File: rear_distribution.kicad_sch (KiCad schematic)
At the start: 42 parts, among them J1 Conn_01x23, J10 Conn_01x02, J11 Conn_01x02, J12 Conn_01x02, J13 Conn_01x04, J14 Conn_01x02, J15 Conn_01x04, J16 Conn_01x23, J17 Conn_01x35, J2 Conn_01x02, J3 Conn_01x02, J4 Conn_01x04, J5 Conn_01x03, J6 Conn_01x08, J7 Conn_01x23, J8 Conn_01x08, J9 Conn_01x08, K1 G2RL-1A, Q1 DMN61D8LQ

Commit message: schematic: Tentatively finish major schematic parts
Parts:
- removed J1: Conn_01x23, yfs:AMPSEAL-23-776087, symbol Connector_Generic:Conn_01x23
- removed NT1: NetTie_4_Cross, symbol Device:NetTie_4_Cross
- removed NT2: NetTie_2, symbol Device:NetTie_2
- removed Q1: DMN61D8LQ, Package_TO_SOT_SMD:SOT-23, symbol Transistor_FET:DMN61D8LQ
- added J21: Conn_01x23, yfs:AMPSEAL-23-776087, symbol Connector_Generic:Conn_01x23
- added NT1: NetTie_2, symbol Device:NetTie_2
- added NT3: NetTie_3_Tee, symbol Device:NetTie_3_Tee
- added Q1, Q4: DMN6075S, Package_TO_SOT_SMD:SOT-23, symbol Transistor_FET:DMN6075S
- added R43, R46, R55, R56: 10k, symbol Device:R_Small
- added R44, R45: 100, symbol Device:R_Small
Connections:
- net +12V: now also NT1.1
- net 12V_BMS: now also J16.5 (Pin_5); no longer J16.19 (Pin_19)
- net 12V_BRAKE_LIGHT: now also F17.2
- net 12V_DTI: now also J21.1 (Pin_1), J21.5 (Pin_5), J21.9 (Pin_9)
- net 12V_FAN: now also J16.4 (Pin_4); no longer J16.20 (Pin_20)
- net 12V_HV_DET: now also J16.3 (Pin_3); no longer J16.21 (Pin_21)
- net 12V_IMD: now also J16.2 (Pin_2); no longer J16.22 (Pin_22)
- net 12V_PRCHG: now also J16.1 (Pin_1); no longer J16.23 (Pin_23)
- net 5V_TSAL: now also J16.6 (Pin_6); no longer J16.18 (Pin_18)
- net AIR+_ACT: now also J16.19 (Pin_19); no longer J16.5 (Pin_5)
- net AIR+_INT: now also J16.18 (Pin_18); no longer J16.6 (Pin_6)
- net AIR-_ACT: now also J16.17 (Pin_17); no longer J16.7 (Pin_7)
- net AIR-_INT: now also J16.16 (Pin_16); no longer J16.8 (Pin_8)
- net BMS_OK: now also J16.10 (Pin_10); no longer J16.14 (Pin_14)
- net BRAKE_SWITCH_IN: now also NT1.2; no longer F17.2
- net CANH: now also J16.7 (Pin_7), J21.12 (Pin_12); no longer J16.17 (Pin_17)
- net CANH_DTI: now also J21.11 (Pin_11)
- net CANL: now also J16.8 (Pin_8), J21.4 (Pin_4); no longer J16.16 (Pin_16)
- net CANL_DTI: now also J21.3 (Pin_3)
- net DISCHG: now also J16.13 (Pin_13); no longer J16.11 (Pin_11)
- net DTI_OK: now also J21.13 (Pin_13)
- net GND: now also J16.21 (Pin_21), J16.22 (Pin_22), J16.23 (Pin_23), J21.16 (Pin_16), J21.17 (Pin_17), NT3.3, Q1.2 (S), Q4.2 (S), R43.2, R46.2; no longer J16.1 (Pin_1), J16.2 (Pin_2), J16.3 (Pin_3)
- net GND_BRAKE_LIGHT: now also Q4.3 (D)
- net GND_COOLANT: now also NT3.1
- net GND_TSAL_LED: now also NT3.2
- net HV_DET: now also J16.20 (Pin_20); no longer J16.4 (Pin_4)
- net IMD_OK: now also J16.11 (Pin_11); no longer J16.13 (Pin_13)
- net MCU_COOLANT: now also R45.1, R46.1
- net PRCHG_ACT: now also J16.15 (Pin_15); no longer J16.9 (Pin_9)
- net PRCHG_INT: now also J16.14 (Pin_14); no longer J16.10 (Pin_10)
- net SDN_TSAC_IN: now also J16.9 (Pin_9); no longer J16.15 (Pin_15)
- net at D1.2 (A), K1.A2: now also Q1.3 (D)
- new net: Q4.1 (G), R44.2
- new net: Q1.1 (G), R45.2
- new net +3V3: R55.1, R56.1
- new net DTI_IN_1: J21.21 (Pin_21)
- new net DTI_IN_2: J21.22 (Pin_22)
- new net DTI_OUT_1: J21.19 (Pin_19), R55.2
- new net DTI_OUT_2: J21.20 (Pin_20), R56.2
- new net MCU_BRAKE: R43.1, R44.1
- no-connect marks 23 -> 19
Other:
- removed sheet Divider10
- removed sheet Divider11
- removed sheet Divider12
- removed sheet Divider13
- removed sheet Divider14
- removed sheet Divider15
- removed sheet Divider16
- removed sheet Divider17
- removed sheet Divider18
- removed sheet Divider19
- removed sheet Divider6
- removed sheet Divider7
- removed sheet Divider8
- removed sheet Divider9
- sheet Divider ports: added IN1, IN2, IN3, IN4, OUT1, OUT2, OUT3, OUT4; removed IN, OUT
- sheet Divider1 ports: added IN1, IN2, IN3, IN4, OUT1, OUT2, OUT3, OUT4; removed IN, OUT
- sheet Divider2 ports: added IN1, IN2, IN3, IN4, OUT1, OUT2, OUT3, OUT4; removed IN, OUT
- sheet Divider3 ports: added IN1, IN2, IN3, IN4, OUT1, OUT2, OUT3, OUT4; removed IN, OUT
- sheet Divider4 ports: added IN1, IN2, IN3, IN4, OUT1, OUT2, OUT3, OUT4; removed IN, OUT
- sheet Divider5 ports: added IN1, IN2, IN3, IN4, OUT1, OUT2, OUT3, OUT4; removed IN, OUT
- sheet Microcontroller ports: added BMS_OK_SAMPLE, DISCHG_SAMPLE, DTI_OK_SAMPLE, IMD_OK_SAMPLE, SDN_FRONT_SAMPLE; removed SDN_DTI_SAMPLE
- note added: "BSPD Input"
- note added: "Brake Light Switching"
- note added: "Coolant Pump Switching"
- note removed: "BSPD"
- note removed: "Brake Light Activation"
- note removed: "Connect any spare MCU GPIO"
- note removed: "Coolant Pump"
- note removed: "Could sample BMS_OK and IMD_OK if spare GPIO"
- note removed: "Measure discharge?"
- note removed: "TODO: Switch to resistor arrays"
- company: (none) -> York Formula Student
- title: (none) -> Rear Distribution
- moved on the sheet: D1, F1, F10, F11, F12, F13, F14, F15, F16, F17, F18, F20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

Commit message: schematic: Re-annotate and add RTC battery
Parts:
- renumbered D1 to D7, F20 to F11, F17 to F12, F18 to F13, F3 to F21, F4 to F22, F5 to F23, F6 to F24, F7 to F25, F8 to F26, F9 to F27, F13 to F31, F14 to F32, F15 to F33, F16 to F34, F1 to F41, F11 to F51, F10 to F61, F12 to F81, F2 to F91, J17 to J11, J7 to J21, J16 to J31, J21 to J41, J9 to J51, J8 to J61, J10 to J71, J11 to J81, J12 to J82, J13 to J83, J15 to J84, J14 to J85, J2 to J91, J3 to J92, J4 to J93, J5 to J94, J6 to J95, JP1 to JP61, NT3 to NT1, NT1 to NT2, Q4 to Q1, Q1 to Q2, R55 to R11, R56 to R12, R43 to R13, R44 to R14, R46 to R15, R45 to R16
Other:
- note removed: "Should MCU measure UPS output directly?"
- moved on the sheet: F51, F61, J51, J61, JP61

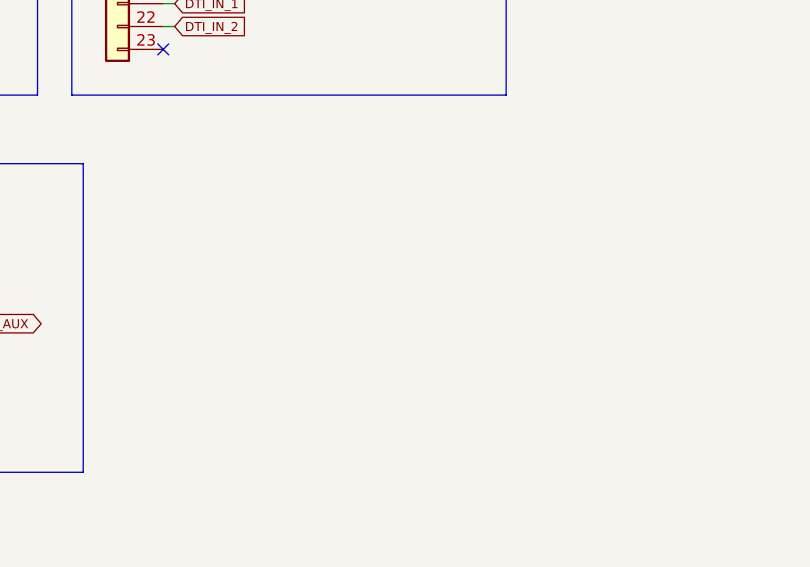
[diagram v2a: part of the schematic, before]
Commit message: schematic: Assign footprints and fill most of BOM
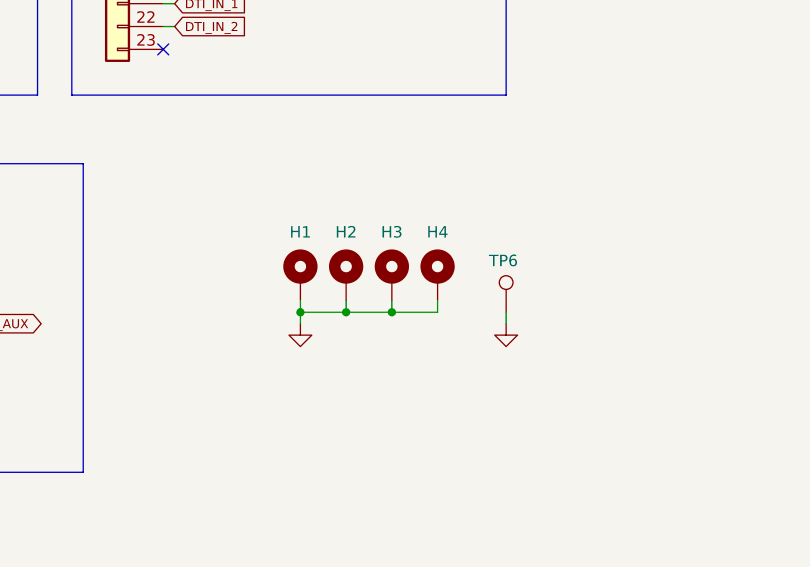
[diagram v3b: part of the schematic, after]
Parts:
- added H1, H2, H3, H4: MountingHole_Pad, MountingHole:MountingHole_3.2mm_M3_Pad_Via, symbol Mechanical:MountingHole_Pad
- added TP6: TestPoint, TestPoint:TestPoint_Keystone_5019_Miniature, symbol Connector:TestPoint
- F11, F12, F13, F21, F22, F23, F24, F25, F26, F27, F31, F32, F33, F34, F41, F51, F61, F81, F91: footprint (none) -> yfs:Keystone_3557-2; DigiKey # (none) -> 36-3557-2-ND; LCSC # (none) -> C352820; Mfr (none) -> Keystone Electronics; Mfr # (none) -> 3557-2; Mouser # (none) -> 534-3557-2
- J11: footprint (none) -> yfs:AMPSEAL-35-776163; DigiKey # (none) -> A106460-ND; Mfr (none) -> TE Connectivity; Mfr # (none) -> 776163-1; Mouser # (none) -> 571-776163-1
- J21, J31, J41: DigiKey # (none) -> A107007-ND; Mfr (none) -> TE Connectivity; Mfr # (none) -> 776087-1; Mouser # (none) -> 571-776087-1
- J51, J61: footprint (none) -> yfs:AMPSEAL-8-776280; DigiKey # (none) -> 776280-1-ND; Mfr (none) -> TE Connectivity; Mfr # (none) -> 776280-1; Mouser # (none) -> 571-776280-1
- J71, J82: footprint (none) -> yfs:MolexMicrofitPlus1x2; DigiKey # (none) -> 900-2157601032-ND; Mfr (none) -> Molex; Mfr # (none) -> 2157601032; Mouser # (none) -> 538-215760-1032
- J81, J91: footprint (none) -> yfs:MolexMicrofitPlus1x2; DigiKey # (none) -> 900-2157601022-ND; Mfr (none) -> Molex; Mfr # (none) -> 2157601022; Mouser # (none) -> 538-215760-1022
- J83, J84, J93: footprint (none) -> yfs:MolexMicrofitPlus1x4; DigiKey # (none) -> 900-2157601004-ND; Mfr (none) -> Molex; Mfr # (none) -> 2157601004; Mouser # (none) -> 538-215760-1004
- J85, J92: footprint (none) -> yfs:MolexMicrofitPlus1x2; DigiKey # (none) -> 900-2157601002-ND; Mfr (none) -> Molex; Mfr # (none) -> 2157601002; Mouser # (none) -> 538-215760-1002
- J94: footprint (none) -> yfs:MolexMicrofitPlus1x3; DigiKey # (none) -> 900-2157601003-ND; Mfr (none) -> Molex; Mfr # (none) -> 2157601003; Mouser # (none) -> 538-215760-1003
- J95: footprint (none) -> yfs:MolexMicrofitPlus1x8; DigiKey # (none) -> 900-2157601008-ND; Mfr (none) -> Molex; Mfr # (none) -> 2157601008; Mouser # (none) -> 538-215760-1008
- JP61: footprint (none) -> Jumper:SolderJumper-2_P1.3mm_Open_RoundedPad1.0x1.5mm
- K1: DigiKey # (none) -> Z140-ND; Mfr (none) -> Omron; Mfr # (none) -> G2RL-1A-DC12; Mouser # (none) -> 653-G2RL-1A-DC12
- NT1: footprint (none) -> NetTie:NetTie-3_SMD_Pad0.5mm
- NT2: footprint (none) -> NetTie:NetTie-2_SMD_Pad0.5mm
- R11, R12, R13, R15: footprint (none) -> Resistor_SMD:R_0603_1608Metric; LCSC # (none) -> C25804; Mfr (none) -> Uni-Royal; Mfr # (none) -> 0603WAF1002T5E
- R14, R16: footprint (none) -> Resistor_SMD:R_0603_1608Metric
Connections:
- net GND: now also H1.1, H2.1, H3.1, H4.1, TP6.1

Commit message: *: Setup PCB
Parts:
- added NT10, NT3, NT4, NT5, NT6, NT7, NT8, NT9: NetTie_2, NetTie:NetTie-2_SMD_Pad0.5mm, symbol Device:NetTie_2
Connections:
- net SDN_AUX_IN: now also NT8.2; no longer J51.3 (Pin_3)
- net SDN_AUX_OUT: now also NT9.1; no longer J11.31 (Pin_31)
- net SDN_BSPD_OUT: now also NT3.1; no longer J21.10 (Pin_10)
- net SDN_FRONT_OUT: now also NT4.1; no longer J82.2 (Pin_2)
- net SDN_HVD_IN: now also NT7.2; no longer J11.32 (Pin_32)
- net SDN_LATCH_OUT: now also NT5.1; no longer J11.35 (Pin_35)
- net SDN_LEFT_ESTOP_OUT: now also NT6.1; no longer J11.33 (Pin_33)
- net SDN_TSAC_IN: now also NT10.2; no longer J11.30 (Pin_30)
- new net SDN_FRONT_IN: J21.10 (Pin_10), NT3.2
- new net SDN_HVD_OUT: J51.3 (Pin_3), NT8.1
- new net SDN_LATCH_IN: J82.2 (Pin_2), NT4.2
- new net SDN_LEFT_ESTOP_IN: J11.35 (Pin_35), NT5.2
- new net SDN_RIGHT_ESTOP_IN: J11.33 (Pin_33), NT6.2
- new net SDN_RIGHT_ESTOP_OUT: J11.32 (Pin_32), NT7.1
- new net SDN_TSMS_IN: J11.31 (Pin_31), NT9.2
- new net SDN_TSMS_OUT: J11.30 (Pin_30), NT10.1
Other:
- moved on the sheet: F11, F12

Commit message: pcb: Add layout progress so far
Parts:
- removed J71: Conn_01x02, yfs:MolexMicrofitPlus1x2, symbol Connector_Generic:Conn_01x02
- removed J84: Conn_01x04, yfs:MolexMicrofitPlus1x4, symbol Connector_Generic:Conn_01x04
- removed R11, R12: 10k, Resistor_SMD:R_0603_1608Metric, symbol Device:R_Small
- renumbered F81 to F71, F91 to F81, J81 to J71, J82 to J72, J83 to J73, J85 to J74, J91 to J81, J92 to J82, J93 to J83, J94 to J84, J95 to J85
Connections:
- net BMS_RESET is gone; now on net SDN_LEFT_ESTOP_IN: J11.13 (Pin_13)
- net IMD_RESET is gone; now on net 12V_COOLANT: J11.12 (Pin_12)
- net +12V: now also F13.1; no longer F13.2
- net 12V_BMS: now also J31.3 (Pin_3); no longer J31.5 (Pin_5)
- net 12V_BRAKE_LIGHT: now also J11.11 (Pin_11); no longer J11.27 (Pin_27)
- net 12V_COOLANT: now also K1.14; no longer J11.29 (Pin_29), K1.13
- net 12V_FAN: now also J31.1 (Pin_1); no longer J31.4 (Pin_4)
- net 12V_HV_DET: now also J31.4 (Pin_4); no longer J31.3 (Pin_3)
- net 12V_PRCHG: now also J31.17 (Pin_17); no longer J31.1 (Pin_1)
- net 12V_TSAL_LED: now also J11.10 (Pin_10); no longer J11.25 (Pin_25)
- net AIR+_ACT: now also J31.7 (Pin_7); no longer J31.19 (Pin_19)
- net AIR+_INT: now also J31.8 (Pin_8); no longer J31.18 (Pin_18)
- net AIR-_ACT: now also J31.15 (Pin_15); no longer J31.17 (Pin_17)
- net AIR-_INT: now also J31.21 (Pin_21); no longer J31.16 (Pin_16)
- net BMS_OK: now also J31.9 (Pin_9); no longer J31.10 (Pin_10)
- net BRAKE_SWITCH_OUT: now also J11.9 (Pin_9); no longer J11.20 (Pin_20)
- net CANH: now also J31.14 (Pin_14); no longer J31.7 (Pin_7)
- net CANL: now also J31.13 (Pin_13); no longer J31.8 (Pin_8)
- net DISCHG: now also J31.12 (Pin_12); no longer J31.13 (Pin_13)
- net GND: now also J31.18 (Pin_18), J31.19 (Pin_19), J31.20 (Pin_20); no longer J11.1 (Pin_1), J11.2 (Pin_2), J11.3 (Pin_3), J11.4 (Pin_4), J31.21 (Pin_21), J31.22 (Pin_22), J31.23 (Pin_23)
- net GND_BRAKE_LIGHT: now also J11.8 (Pin_8); no longer J11.26 (Pin_26)
- net HV_DET: now also J31.5 (Pin_5); no longer J31.20 (Pin_20)
- net IMD_OK: now also J31.10 (Pin_10); no longer J31.11 (Pin_11)
- net IMD_PWM: now also J31.11 (Pin_11); no longer J31.12 (Pin_12)
- net PRCHG_ACT: now also J31.22 (Pin_22); no longer J31.15 (Pin_15)
- net PRCHG_INT: now also J31.23 (Pin_23); no longer J31.14 (Pin_14)
- net SDN_AUX_IN: now also J61.5 (Pin_5); no longer J61.4 (Pin_4)
- net SDN_AUX_OUT: now also J61.4 (Pin_4); no longer J61.5 (Pin_5)
- net SDN_BSPD_OUT: now also J11.2 (Pin_2); no longer J11.11 (Pin_11)
- net SDN_LEFT_ESTOP_IN: no longer J11.35 (Pin_35)
- net SDN_LEFT_ESTOP_OUT: now also J11.4 (Pin_4); no longer J11.34 (Pin_34)
- net SDN_RIGHT_ESTOP_IN: now also J11.3 (Pin_3); no longer J11.33 (Pin_33)
- net SDN_RIGHT_ESTOP_OUT: now also J11.1 (Pin_1); no longer J11.32 (Pin_32)
- net SDN_TSAC_IN: now also J31.16 (Pin_16); no longer J31.9 (Pin_9)
- net SDN_TSMS_IN: now also J11.5 (Pin_5); no longer J11.31 (Pin_31)
- net SDN_TSMS_OUT: now also J11.6 (Pin_6); no longer J11.30 (Pin_30)
- net TSAL_GREEN: now also J11.20 (Pin_20); no longer J11.24 (Pin_24)
- net DTI_IN_1: no longer names the net of J41.21 (Pin_21)
- net DTI_IN_2: no longer names the net of J41.22 (Pin_22)
- net DTI_OUT_1: no longer names the net of J41.19 (Pin_19)
- net DTI_OUT_2: no longer names the net of J41.20 (Pin_20)
- new net 12V_COOLANT_IN: F13.2, K1.13
- no-connect marks 19 -> 21
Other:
- sheet Microcontroller ports: added 12V_BRAKE_LIGHT_SAMPLE; removed 12V_AUX_SAMPLE
- note removed: "BSPD Input"
- moved on the sheet: F13

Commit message: *: Tentatively finish everything
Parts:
- removed NT1: NetTie_3_Tee, NetTie:NetTie-3_SMD_Pad0.5mm, symbol Device:NetTie_3_Tee
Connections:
- net GND_TSAL_LED is gone; now on net BRAKE_SWITCH_IN: J11.22 (Pin_22)
- net +12V: now also J11.17 (Pin_17), J11.18 (Pin_18), J11.19 (Pin_19), J11.20 (Pin_20), J11.21 (Pin_21); no longer J11.14 (Pin_14), J11.15 (Pin_15), J11.16 (Pin_16)
- net BMS_OK: now also J73.2 (Pin_2); no longer J73.4 (Pin_4)
- net BRAKE_SWITCH_IN: no longer J11.21 (Pin_21)
- net DTI_OK: now also J73.4 (Pin_4); no longer J73.2 (Pin_2)
- net GND: now also J11.29 (Pin_29), J11.30 (Pin_30), J11.31 (Pin_31), J11.32 (Pin_32), J11.33 (Pin_33), J11.34 (Pin_34)
- net TSAL_GREEN: now also J11.35 (Pin_35); no longer J11.20 (Pin_20)
- net GND_COOLANT: no longer names the net of J11.28 (Pin_28)
- no-connect marks 21 -> 22

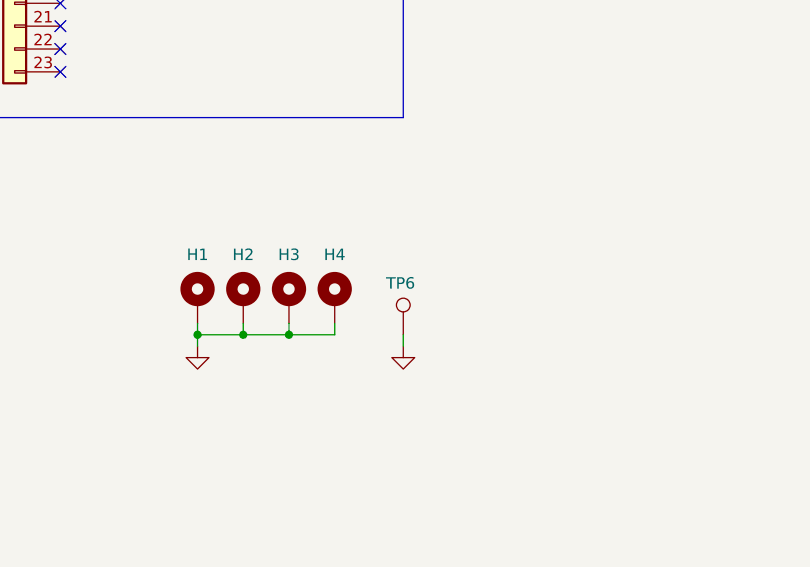
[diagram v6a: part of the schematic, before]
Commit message: *: Add CAN test points
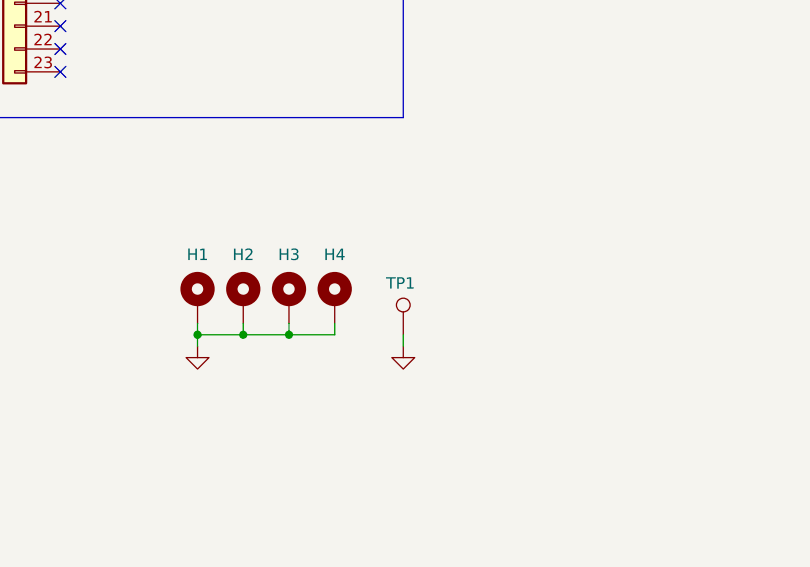
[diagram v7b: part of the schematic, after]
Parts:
- renumbered TP6 to TP1
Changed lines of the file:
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@@
 		(on_board yes)
 		(dnp no)
-		(property "Reference" "TP6"
+		(property "Reference" "TP1"
 			(at 241.935 123.825 0)
 			(effects
@@
 			(project "rear_distribution"
 				(path "/f2809c69-a8f9-4542-bde7-ba954770c514"
-					(reference "TP6")
+					(reference "TP1")
 					(unit 1)
 				)

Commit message: schematic: Cleanup root schematic page
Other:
- note added: "MCU Sampling"
- moved on the sheet: D7, F11, F12, F13, F21, F22, F23, F24, F25, F26, F27, F31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
